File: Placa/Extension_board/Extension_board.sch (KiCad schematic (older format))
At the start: 10 parts, among them J1 USB_B_Micro, J2 USB_B_Micro, J3 Conn_01x06_Male, SW1 SW_PUSHBUTTON, U1 STEVAL-STLCS01V1

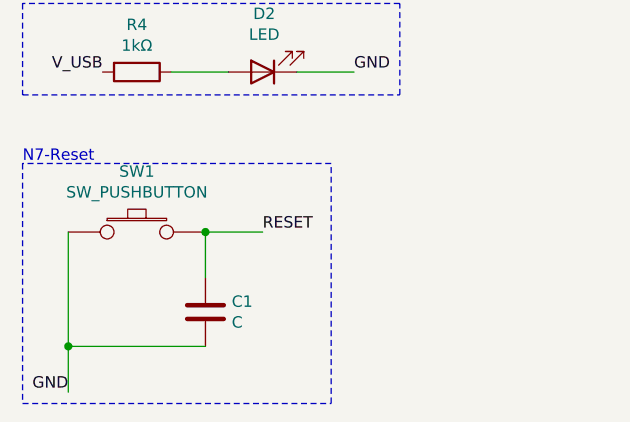
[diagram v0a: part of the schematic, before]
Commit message: Creacion de app en Qt
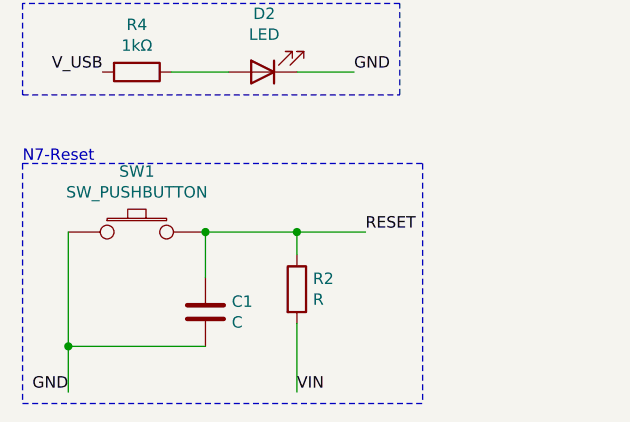
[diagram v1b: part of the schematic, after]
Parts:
- added R2: R, Resistor_SMD:R_0805_2012Metric, symbol Device:R
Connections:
- net RESET: now also R2.1
- net VIN: now also R2.2
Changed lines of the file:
@@
 	1150 6650 1150 6850
 Connection ~ 1150 6650
-Text Label 2000 6150 0    50   ~ 0
+Text Label 2450 6150 0    50   ~ 0
 RESET
-Wire Wire Line
-	1750 6150 2000 6150
-Connection ~ 1750 6150
 Wire Notes Line
 	950  5850 950  6900
-Wire Notes Line
-	950  6900 2300 6900
-Wire Notes Line
-	2300 6900 2300 5850
-Wire Notes Line
-	2300 5850 950  5850
 Text Notes 950  5850 0    50   ~ 0
 N7-Reset
 NoConn ~ 1950 1850
 NoConn ~ 1600 3400
+Wire Wire Line
+	1750 6150 2150 6150
+Connection ~ 1750 6150
+$Comp
+L Device:R R2
+U 1 1 612FAF61
+P 2150 6400
+F 0 "R2" H 2220 6446 50  0000 L CNN
+F 1 "R" H 2220 6355 50  0000 L CNN
+F 2 "Resistor_SMD:R_0805_2012Metric" V 2080 6400 50  0001 C CNN
+F 3 "~" H 2150 6400 50  0001 C CNN
+	1    2150 6400
+	1    0    0    -1
+$EndComp
+Text Label 2150 6850 0    50   ~ 0
+VIN
+Wire Wire Line
+	2150 6250 2150 6150
+Connection ~ 2150 6150
+Wire Wire Line
+	2150 6150 2450 6150
+Wire Wire Line
+	2150 6550 2150 6850
+Wire Notes Line
+	2700 5850 2700 6900
+Wire Notes Line
+	950  6900 2700 6900
+Wire Notes Line
+	950  5850 2700 5850
 $EndSCHEMATC
